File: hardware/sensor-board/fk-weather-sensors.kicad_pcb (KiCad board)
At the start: 2 copper layers, 14.2 x 21.6 mm, 10 parts, among them J1 CONN_01X06, U1 MPL3115A2, U2 TSL2591, U3 SHT31

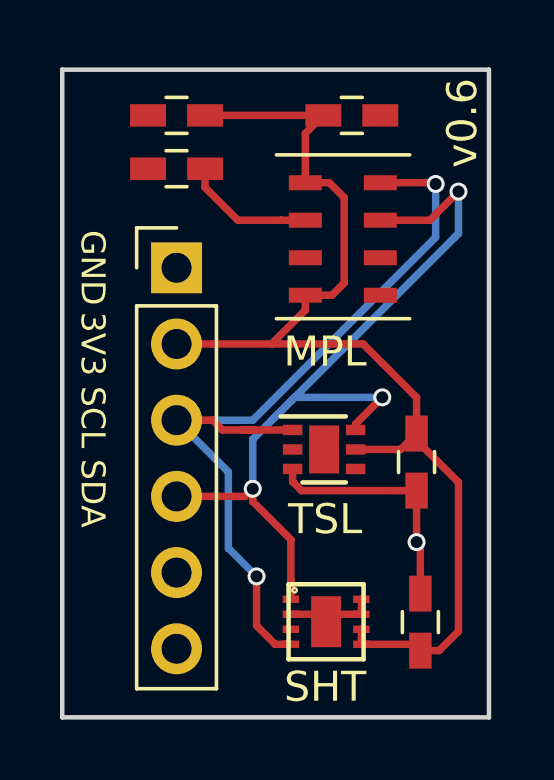
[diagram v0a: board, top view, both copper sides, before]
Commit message: Fix TSL2591 footprint.
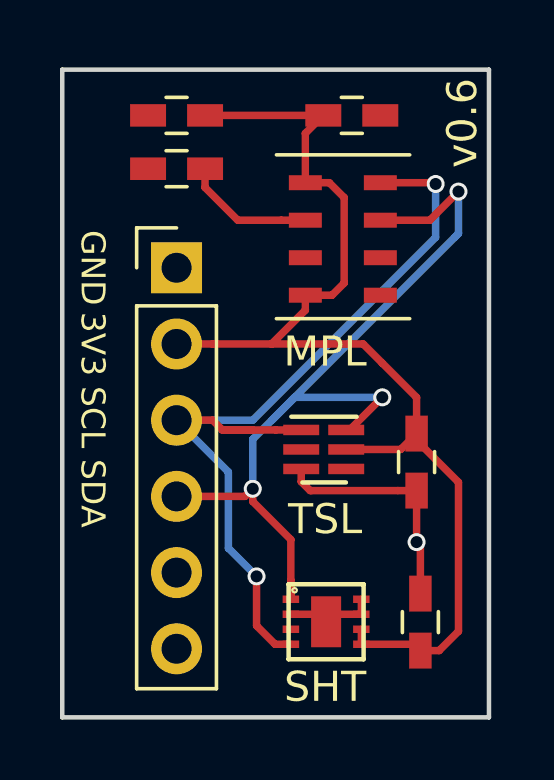
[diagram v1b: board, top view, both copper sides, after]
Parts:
- U2: footprint Housings_DFN_QFN:DFN-6-1EP_2x2mm_Pitch0.65mm -> conservify:TSL2591
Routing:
- net /SCL: track 28.5 -> 29.8 mm
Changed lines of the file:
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@@
     (links 27)
     (no_connects 0)
-    (area 139.492667 99.154 167.362 127.193)
+    (area 140.640999 104.064999 155.015001 125.805001)
     (thickness 1.6)
     (drawings 14)
-    (tracks 84)
+    (tracks 86)
     (zones 0)
     (modules 10)
@@
       (net 4 /SCL) (solder_mask_margin 0.1) (clearance 0.1))
     (model ${KISYS3DMOD}/Housings_DFN_QFN.3dshapes/DFN-8-1EP_6x5mm_Pitch1.27mm.wrl
-      (at (xyz 0 0 0))
-      (scale (xyz 1 1 1))
-      (rotate (xyz 0 0 0))
-    )
-  )
-  (module Housings_DFN_QFN:DFN-6-1EP_2x2mm_Pitch0.65mm (layer F.Cu)
-    (at 149.445 116.7996)
-    (descr "6-Lead Plastic Dual Flat, No Lead Package (MA) - 2x2x0.9 mm Body [DFN] (see Microchip Packaging Specification 00000049BS.pdf)")
-    (tags "DFN 0.65")
-    (attr smd)
-    (fp_text reference U2 (at 0 -2.025) (layer F.SilkS) hide
-      (effects (font (size 1 1) (thickness 0.15)))
-    )
-    (fp_text value TSL2591 (at 0 2.025) (layer F.Fab) hide
-      (effects (font (size 1 1) (thickness 0.15)))
-    )
-    (fp_line (start 0 -1) (end 1 -1) (layer F.Fab) (width 0.15))
-    (fp_line (start 1 -1) (end 1 1) (layer F.Fab) (width 0.15))
-    (fp_line (start 1 1) (end -1 1) (layer F.Fab) (width 0.15))
-    (fp_line (start -1 1) (end -1 0) (layer F.Fab) (width 0.15))
-    (fp_line (start -1 0) (end 0 -1) (layer F.Fab) (width 0.15))
-    (fp_line (start -1.65 -1.25) (end -1.65 1.25) (layer F.CrtYd) (width 0.05))
-    (fp_line (start 1.65 -1.25) (end 1.65 1.25) (layer F.CrtYd) (width 0.05))
-    (fp_line (start -1.65 -1.25) (end 1.65 -1.25) (layer F.CrtYd) (width 0.05))
-    (fp_line (start -1.65 1.25) (end 1.65 1.25) (layer F.CrtYd) (width 0.05))
-    (fp_line (start -0.725 1.1) (end 0.725 1.1) (layer F.SilkS) (width 0.15))
-    (fp_line (start -1.45 -1.1) (end 0.725 -1.1) (layer F.SilkS) (width 0.15))
-    (pad 1 smd rect (at -1.05 -0.65) (size 0.65 0.35) (layers F.Cu F.Paste F.Mask)
-      (net 4 /SCL))
-    (pad 2 smd rect (at -1.05 0) (size 0.65 0.35) (layers F.Cu F.Paste F.Mask)
-      (net 8 "Net-(U2-Pad2)"))
-    (pad 3 smd rect (at -1.05 0.65) (size 0.65 0.35) (layers F.Cu F.Paste F.Mask)
-      (net 2 GND))
-    (pad 4 smd rect (at 1.05 0.65) (size 0.65 0.35) (layers F.Cu F.Paste F.Mask)
-      (net 9 "Net-(U2-Pad4)"))
-    (pad 5 smd rect (at 1.05 0) (size 0.65 0.35) (layers F.Cu F.Paste F.Mask)
-      (net 3 3V3))
-    (pad 6 smd rect (at 1.05 -0.65) (size 0.65 0.35) (layers F.Cu F.Paste F.Mask)
-      (net 5 /SDA))
-    (pad 7 smd rect (at 0 0.4) (size 1 0.8) (layers F.Cu F.Paste F.Mask)
-      (solder_paste_margin_ratio -0.2))
-    (pad 7 smd rect (at 0 -0.4) (size 1 0.8) (layers F.Cu F.Paste F.Mask)
-      (solder_paste_margin_ratio -0.2))
-    (model ${KISYS3DMOD}/Housings_DFN_QFN.3dshapes/DFN-6-1EP_2x2mm_Pitch0.65mm.wrl
       (at (xyz 0 0 0))
       (scale (xyz 1 1 1))
@@
       (xy -6.476371 1.79874)) (layer B.SilkS) (width 0.01))
   )
+  (module conservify:TSL2591 (layer F.Cu)
+    (at 149.445 116.7996)
+    (descr "6-Lead Plastic Dual Flat, No Lead Package (MA) - 2x2x0.9 mm Body [DFN] (see Microchip Packaging Specification 00000049BS.pdf)")
+    (tags "DFN 0.65")
+    (attr smd)
+    (fp_text reference U2 (at 0 -2.025) (layer F.SilkS) hide
+      (effects (font (size 1 1) (thickness 0.15)))
+    )
+    (fp_text value TSL2591 (at -0.9992 -2.0574) (layer F.Fab)
+      (effects (font (size 1 1) (thickness 0.15)))
+    )
+    (fp_line (start 0 -1) (end 1 -1) (layer F.Fab) (width 0.15))
+    (fp_line (start 1 -1) (end 1 1) (layer F.Fab) (width 0.15))
+    (fp_line (start 1 1) (end -1 1) (layer F.Fab) (width 0.15))
+    (fp_line (start -1 1) (end -1 0) (layer F.Fab) (width 0.15))
+    (fp_line (start -1 0) (end 0 -1) (layer F.Fab) (width 0.15))
+    (fp_line (start -1.65 -1.25) (end -1.65 1.25) (layer F.CrtYd) (width 0.05))
+    (fp_line (start 1.65 -1.25) (end 1.65 1.25) (layer F.CrtYd) (width 0.05))
+    (fp_line (start -1.65 -1.25) (end 1.65 -1.25) (layer F.CrtYd) (width 0.05))
+    (fp_line (start -1.65 1.25) (end 1.65 1.25) (layer F.CrtYd) (width 0.05))
+    (fp_line (start -0.725 1.1) (end 0.725 1.1) (layer F.SilkS) (width 0.15))
+    (fp_line (start -1.0922 -1.0922) (end 1.0828 -1.0922) (layer F.SilkS) (width 0.15))
+    (pad 1 smd rect (at -0.7634 -0.65) (size 1.2 0.35) (layers F.Cu F.Paste F.Mask)
+      (net 4 /SCL))
+    (pad 2 smd rect (at -0.7634 0) (size 1.2 0.35) (layers F.Cu F.Paste F.Mask)
+      (net 8 "Net-(U2-Pad2)"))
+    (pad 3 smd rect (at -0.7634 0.65) (size 1.2 0.35) (layers F.Cu F.Paste F.Mask)
+      (net 2 GND))
+    (pad 4 smd rect (at 0.7366 0.65) (size 1.2 0.35) (layers F.Cu F.Paste F.Mask)
+      (net 9 "Net-(U2-Pad4)"))
+    (pad 5 smd rect (at 0.7366 0) (size 1.2 0.35) (layers F.Cu F.Paste F.Mask)
+      (net 3 3V3))
+    (pad 6 smd rect (at 0.7366 -0.65) (size 1.2 0.35) (layers F.Cu F.Paste F.Mask)
+      (net 5 /SDA))
+    (model ${KISYS3DMOD}/Housings_DFN_QFN.3dshapes/DFN-6-1EP_2x2mm_Pitch0.65mm.wrl
+      (at (xyz 0 0 0))
+      (scale (xyz 1 1 1))
+      (rotate (xyz 0 0 0))
+    )
+  )
   (dimension 21.59 (width 0.3) (layer Dwgs.User)
     (gr_text "21.590 mm" (at 160.862 114.935 270) (layer Dwgs.User)
@@
   (segment (start 145.476 108.067) (end 146.5674 109.1584) (width 0.25) (layer F.Cu) (net 1))
   (segment (start 148.0186 109.1584) (end 148.8186 109.1584) (width 0.25) (layer F.Cu) (net 1))
+  (segment (start 149.0218 118.171) (end 151.902 118.171) (width 0.25) (layer F.Cu) (net 2))
+  (segment (start 148.6816 117.4496) (end 148.6816 117.8746) (width 0.25) (layer F.Cu) (net 2))
+  (segment (start 148.6816 117.8746) (end 148.978 118.171) (width 0.25) (layer F.Cu) (net 2))
+  (segment (start 148.978 118.171) (end 149.0218 118.171) (width 0.25) (layer F.Cu) (net 2))
   (segment (start 152.527 118.171) (end 152.527 119.888) (width 0.25) (layer F.Cu) (net 2))
   (segment (start 152.654 121.605) (end 152.654 120.015) (width 0.25) (layer F.Cu) (net 2))
   (segment (start 152.654 120.015) (end 152.527 119.888) (width 0.25) (layer F.Cu) (net 2))
   (via (at 152.527 119.888) (size 0.6) (drill 0.4) (layers F.Cu B.Cu) (net 2))
-  (segment (start 148.395 117.4496) (end 148.395 117.8746) (width 0.25) (layer F.Cu) (net 2))
-  (segment (start 148.395 117.8746) (end 148.6914 118.171) (width 0.25) (layer F.Cu) (net 2))
-  (segment (start 148.6914 118.171) (end 151.902 118.171) (width 0.25) (layer F.Cu) (net 2))
   (segment (start 151.902 118.171) (end 152.527 118.171) (width 0.25) (layer F.Cu) (net 2))
   (segment (start 148.336 122.293) (end 149.261 122.293) (width 0.25) (layer F.Cu) (net 2))
@@
   (segment (start 150.686 122.293) (end 149.761 122.293) (width 0.25) (layer F.Cu) (net 2))
   (segment (start 149.761 122.293) (end 149.511 122.543) (width 0.25) (layer F.Cu) (net 2))
+  (segment (start 150.1816 116.7996) (end 151.9984 116.7996) (width 0.25) (layer F.Cu) (net 3))
+  (segment (start 151.9984 116.7996) (end 152.527 116.271) (width 0.25) (layer F.Cu) (net 3))
   (segment (start 148.8186 107.9084) (end 149.6186 107.9084) (width 0.25) (layer F.Cu) (net 3))
   (segment (start 149.6186 107.9084) (end 150.114 108.4038) (width 0.25) (layer F.Cu) (net 3))
@@
   (segment (start 152.442 123.293) (end 152.654 123.505) (width 0.25) (layer F.Cu) (net 3))
   (segment (start 150.686 122.793) (end 150.686 123.293) (width 0.25) (layer F.Cu) (net 3))
-  (segment (start 152.527 116.271) (end 151.9984 116.7996) (width 0.25) (layer F.Cu) (net 3))
-  (segment (start 151.9984 116.7996) (end 150.495 116.7996) (width 0.25) (layer F.Cu) (net 3))
+  (segment (start 148.6816 116.1496) (end 147.8316 116.1496) (width 0.25) (layer F.Cu) (net 4))
+  (segment (start 147.8316 116.1496) (end 146.053681 116.1496) (width 0.25) (layer F.Cu) (net 4))
   (segment (start 153.162 107.95) (end 153.162 109.728) (width 0.25) (layer B.Cu) (net 4))
   (segment (start 153.162 109.728) (end 147.066 115.824) (width 0.25) (layer B.Cu) (net 4))
@@
   (via (at 147.193 121.031) (size 0.6) (drill 0.4) (layers F.Cu B.Cu) (net 4))
   (segment (start 146.7404 116.1496) (end 147.066 116.1496) (width 0.25) (layer F.Cu) (net 4))
-  (segment (start 147.066 116.1496) (end 148.395 116.1496) (width 0.25) (layer F.Cu) (net 4))
   (segment (start 144.526 115.824) (end 145.728081 115.824) (width 0.25) (layer F.Cu) (net 4))
   (segment (start 145.728081 115.824) (end 146.053681 116.1496) (width 0.25) (layer F.Cu) (net 4))
@@
   (segment (start 153.1204 107.9084) (end 153.162 107.95) (width 0.25) (layer F.Cu) (net 4))
   (via (at 153.162 107.95) (size 0.6) (drill 0.4) (layers F.Cu B.Cu) (net 4))
+  (segment (start 150.1816 116.1496) (end 150.2964 116.1496) (width 0.25) (layer F.Cu) (net 5))
+  (segment (start 150.2964 116.1496) (end 151.384 115.062) (width 0.25) (layer F.Cu) (net 5))
   (segment (start 147.066 118.11) (end 147.066 118.534264) (width 0.25) (layer F.Cu) (net 5))
   (segment (start 147.066 118.534264) (end 148.336 119.804264) (width 0.25) (layer F.Cu) (net 5))
@@
   (segment (start 152.9696 109.1584) (end 153.924 108.204) (width 0.25) (layer F.Cu) (net 5))
   (via (at 153.924 108.204) (size 0.6) (drill 0.4) (layers F.Cu B.Cu) (net 5))
-  (segment (start 150.495 116.1496) (end 150.495 115.951) (width 0.25) (layer F.Cu) (net 5))
-  (segment (start 150.495 115.951) (end 151.384 115.062) (width 0.25) (layer F.Cu) (net 5))
   (segment (start 148.336 121.793) (end 148.336 121.418) (width 0.25) (layer F.Cu) (net 5))
   (segment (start 148.33741 115.189) (end 147.70241 115.824) (width 0.25) (layer B.Cu) (net 5))

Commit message: Plotting new gerbers. Bump version.
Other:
- board text added: "v0.7"
- board text removed: "v0.6"
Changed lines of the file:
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@@
   (general
     (links 27)
-    (no_connects 0)
-    (area 140.640999 104.064999 155.015001 125.805001)
+    (no_connects 6)
+    (area 139.492667 99.154 167.362 127.193)
     (thickness 1.6)
     (drawings 14)
@@
     (visible_elements FFFFFF7F)
     (pcbplotparams
-      (layerselection 0x0003c_80000001)
+      (layerselection 0x000fc_80000001)
       (usegerberextensions false)
       (excludeedgelayer true)
@@
     (arrow2b (pts (xy 140.716 101.854) (xy 141.842504 101.267579)))
   )
-  (gr_text v0.6 (at 154.051 105.918 90) (layer F.SilkS)
+  (gr_text v0.7 (at 154.051 105.918 90) (layer F.SilkS)
     (effects (font (size 1 1) (thickness 0.15)))
   )
